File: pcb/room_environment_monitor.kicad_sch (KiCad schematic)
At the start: 31 parts, among them J1 Conn_01x02_Pin, J3 Conn_01x06_Socket, P1 USB_C_Plug_USB2.0, Q3 BSS138, SW1 SW_SPST, U2 ESP32-C3-MINI-1, U5 AP2112K-3.3

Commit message: update fab
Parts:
- C10: value 10u -> 1u
- C11: value 22u -> 1u
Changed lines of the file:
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@@
   (symbol (lib_id "Device:C_Small") (at 17.78 32.385 0) (unit 1)
     (in_bom yes) (on_board yes) (dnp no)
-    (property "Reference" "C10" (at 20.32 32.385 0)
+    (property "Reference" "C10" (at 19.685 32.385 0)
       (effects (font (size 1.27 1.27)) (justify left))
     )
-    (property "Value" "10u" (at 20.32 34.925 0)
+    (property "Value" "1u" (at 19.685 34.925 0)
       (effects (font (size 1.27 1.27)) (justify left))
     )
@@
       (effects (font (size 1.27 1.27)) (justify left))
     )
-    (property "Value" "22u" (at 41.91 34.925 0)
+    (property "Value" "1u" (at 41.91 34.925 0)
       (effects (font (size 1.27 1.27)) (justify left))
     )

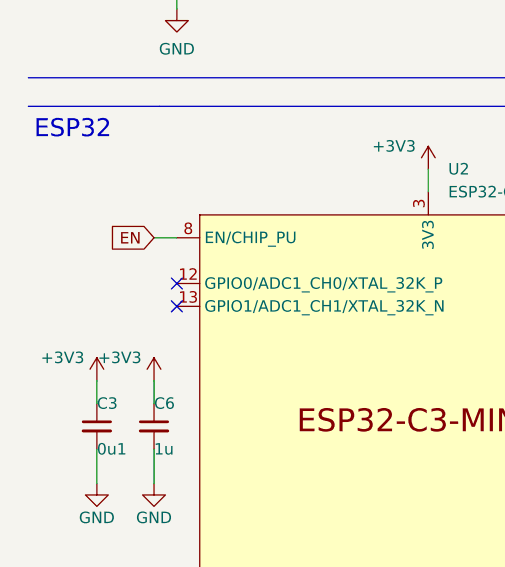
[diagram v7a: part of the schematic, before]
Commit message: add the routing for hte PM1006K enable, and other fixes
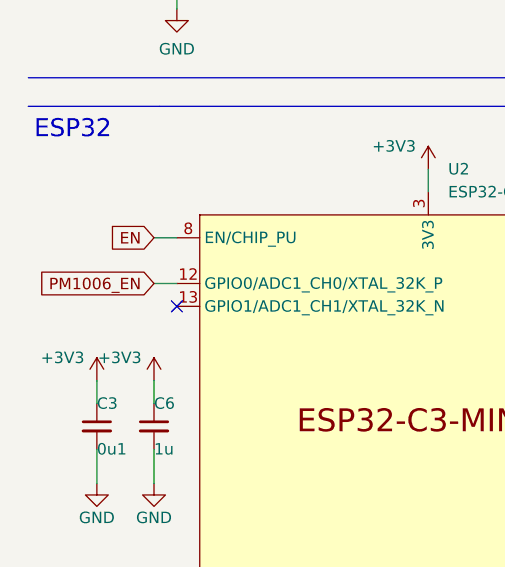
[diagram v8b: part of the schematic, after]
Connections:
- net PM1006_EN: now reaches U2.12 (GPIO0/ADC1_CH0/XTAL_32K_P)
- no-connect marks 8 -> 7
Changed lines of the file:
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@@
   (no_connect (at 84.455 77.47))
   (no_connect (at 41.91 162.56))
-  (no_connect (at 28.575 69.85))
   (wire (pts (xy 84.455 105.41) (xy 90.805 105.41))
     (stroke (width 0) (type default))
@@
   )
   (wire (pts (xy 36.195 26.035) (xy 36.195 28.575))
+    (stroke (width 0) (type default))
+  )
+  (wire (pts (xy 26.035 69.85) (xy 28.575 69.85))
     (stroke (width 0) (type default))
   )
@@
     )
   )
+  (global_label "PM1006_EN" (shape input) (at 26.035 69.85 180) (fields_autoplaced)
+    (effects (font (size 1.27 1.27)) (justify right))
+    (property "Intersheetrefs" "${INTERSHEET_REFS}" (at 12.0433 69.85 0)
+      (effects (font (size 1.27 1.27)) (justify right) hide)
+    )
+  )
